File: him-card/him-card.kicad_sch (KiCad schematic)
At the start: 12 parts, among them J1 Conn_01x03, J3 Conn_01x04, SW1 Init, SW2 Reset

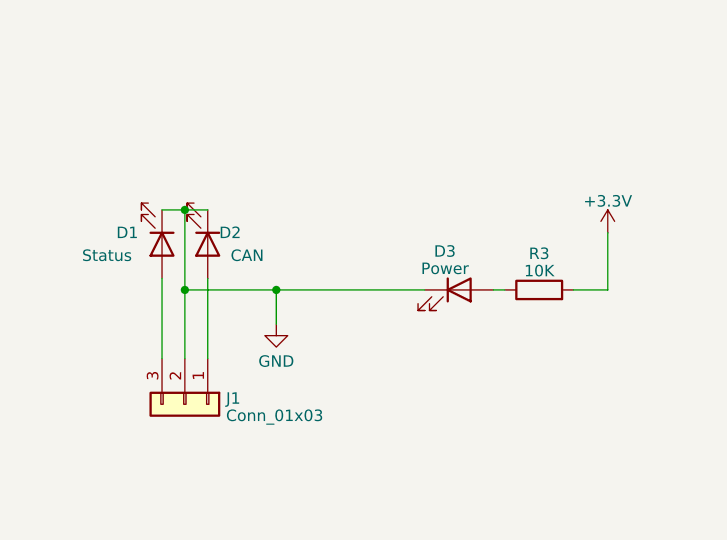
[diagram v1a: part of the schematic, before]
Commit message: Defined status LED colors
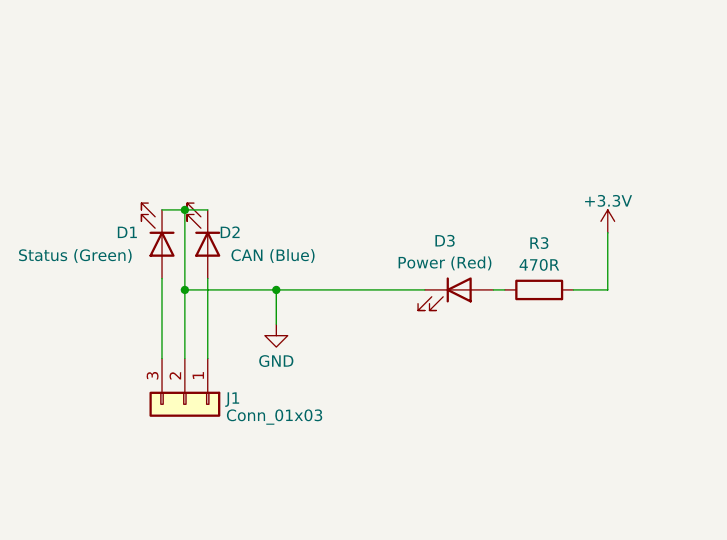
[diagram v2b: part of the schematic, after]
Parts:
- D1: value Status -> Status (Green)
- D2: value CAN -> CAN (Blue)
- D3: value Power -> Power (Red)
- R3: value 10K -> 470R
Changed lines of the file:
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@@
 		(fields_autoplaced yes)
 		(property "Reference" "R3"
-			(at 107.95 93.7641 90)
-			(show_name no)
-			(do_not_autoplace no)
-			(effects
-				(font
-					(size 1.27 1.27)
-				)
-			)
-		)
-		(property "Value" "10K"
-			(at 107.95 95.6851 90)
+			(at 107.95 92.6295 90)
+			(show_name no)
+			(do_not_autoplace no)
+			(effects
+				(font
+					(size 1.27 1.27)
+				)
+			)
+		)
+		(property "Value" "470R"
+			(at 107.95 95.0538 90)
 			(show_name no)
 			(do_not_autoplace no)
@@
 			)
 		)
-		(property "Value" "Status"
-			(at 57.15 93.98 90)
+		(property "Value" "Status (Green)"
+			(at 50.038 93.98 90)
 			(show_name no)
 			(do_not_autoplace no)
@@
 			)
 		)
-		(property "Value" "CAN"
+		(property "Value" "CAN (Blue)"
 			(at 73.66 93.98 90)
 			(show_name no)
@@
 		(fields_autoplaced yes)
 		(property "Reference" "D3"
-			(at 97.4725 93.5101 0)
-			(show_name no)
-			(do_not_autoplace no)
-			(effects
-				(font
-					(size 1.27 1.27)
-				)
-			)
-		)
-		(property "Value" "Power"
-			(at 97.4725 95.4311 0)
-			(show_name no)
-			(do_not_autoplace no)
+			(at 97.4725 92.3755 0)
+			(show_name no)
+			(do_not_autoplace no)
+			(effects
+				(font
+					(size 1.27 1.27)
+				)
+			)
+		)
+		(property "Value" "Power (Red)"
+			(at 97.4725 94.7998 0)
+			(show_name no)
+			(do_not_autoplace no)
